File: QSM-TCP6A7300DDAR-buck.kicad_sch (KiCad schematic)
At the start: 32 parts, among them J1 691322310002, J2 691322310002, J3 BM02B-SRSS-TB LFSN, U1 TCP6A7300DDAR

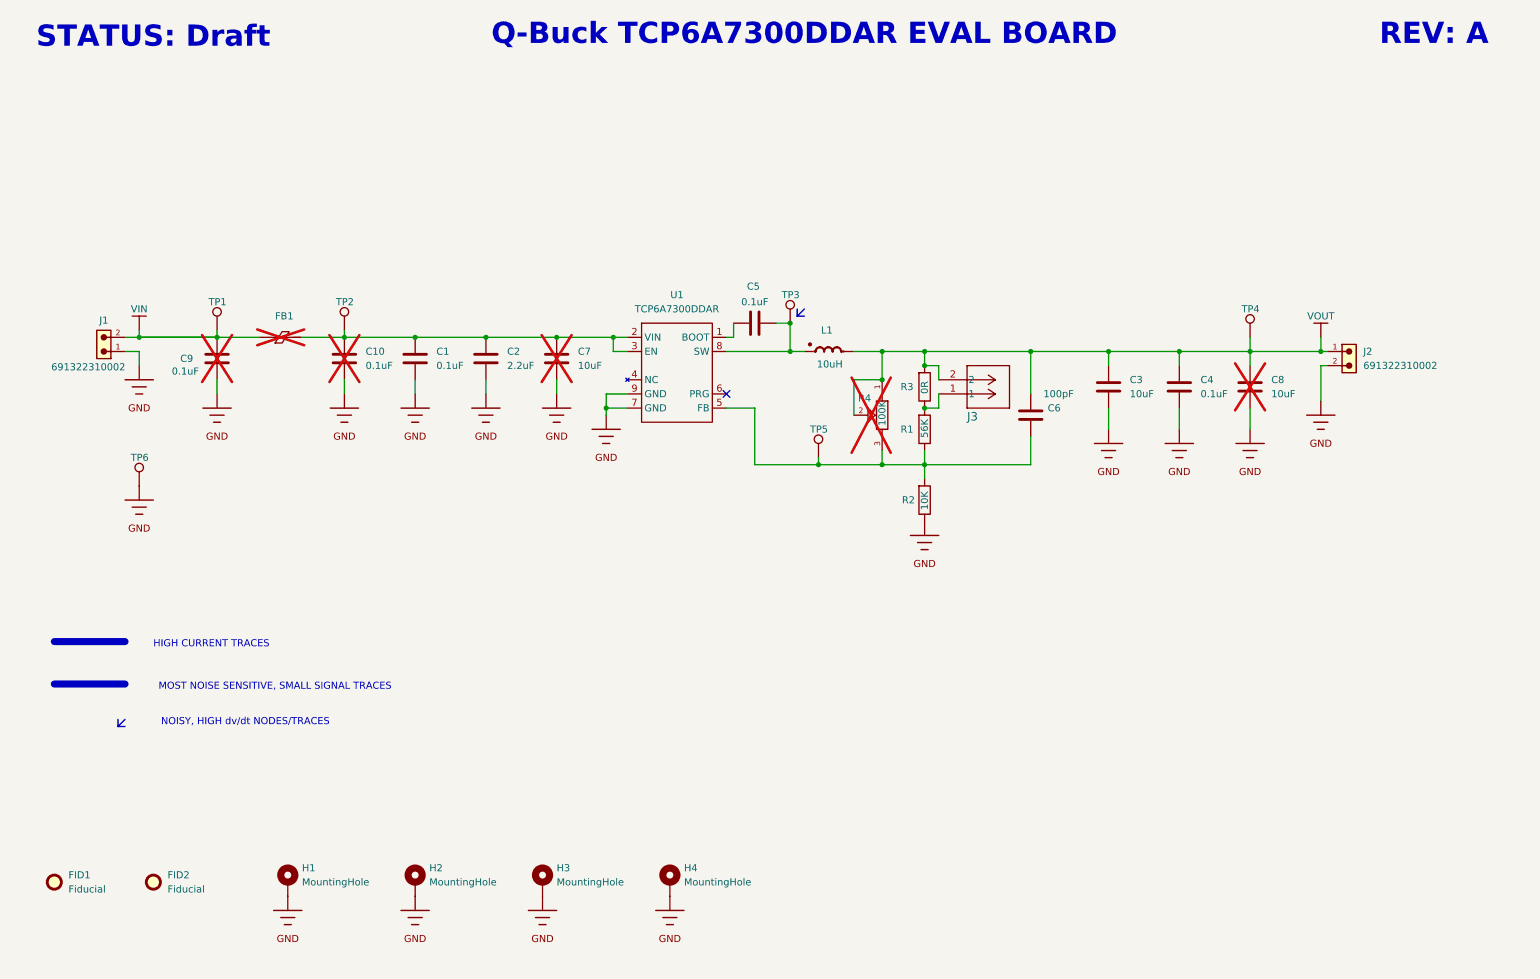
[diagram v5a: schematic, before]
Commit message: chore(project): preparación para manufactura (BOM, stackup PCB y docs)
Documentación (README):
- Refactorización de la narrativa del proyecto enfocándose en la validación empírica y el desarrollo de la industria nacional.
- Integración de la sección 'Design for Testability' (DFT) y justificación técnica del stackup de 4 capas.

Layout (PCB):
- Adición de las tablas de características de la placa y detalles del stackup (capas, grosores de FR4/Prepreg y cobre) en la capa de dibujo para referencia del fabricante.

Proyecto y Esquemático:
- Ajuste y actualización de los metadatos de los componentes para habilitar una generación de BOM limpia y automatizada.
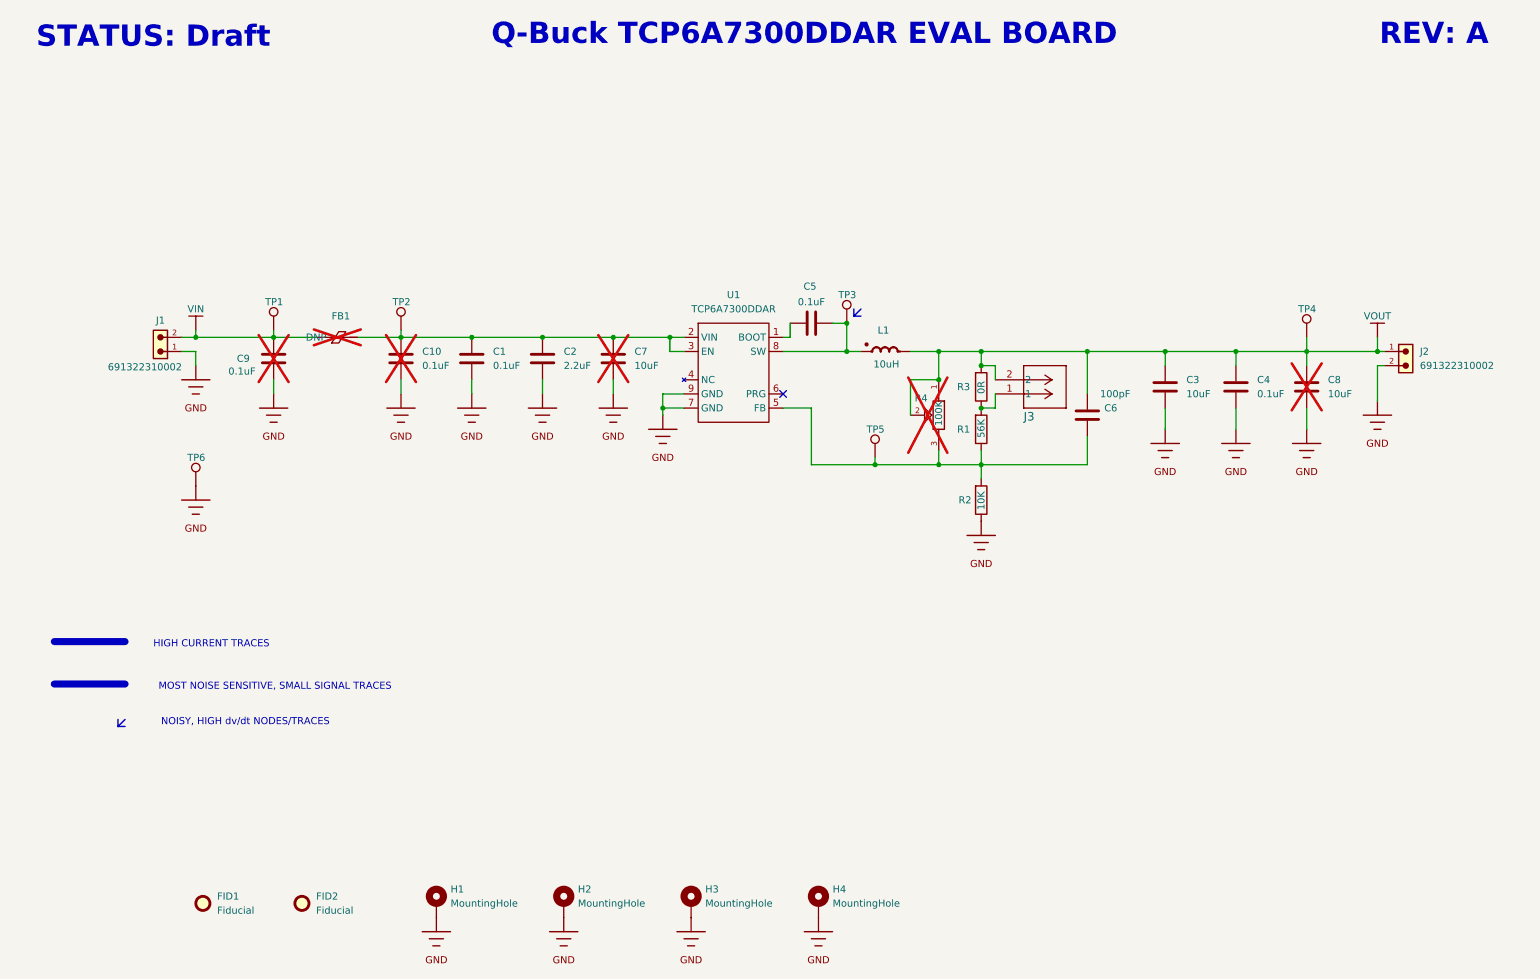
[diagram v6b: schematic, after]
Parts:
- FB1: value (none) -> DNP; Part number (none) -> DNP
- FID1, FID2, H1, H2, H3, H4, TP1, TP2, TP3, TP4, TP5, TP6: Part number (none) -> NA; now left out of the parts list
- J1, J2: Part number (none) -> 691322310002
- L1: Supplier 1 (none) -> https://uelectronics.com/producto/indutor-de-ferrita-10uh-1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
- R2: Supplier 1 (none) -> https://uelectronics.com/producto/resistor-10k-ohm-1-8w-smd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
- R3: Supplier 1 (none) -> https://uelectronics.com/producto/resistor-0-ohm-1-8w-smd-0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
- U1: Part number (none) -> TCP6A7300DDAR
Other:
- moved on the sheet: C1, C10, C2, C3, C4, C5, C6, C7, C8, C9, FB1, FID1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
